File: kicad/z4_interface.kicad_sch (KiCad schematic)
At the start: 0 parts

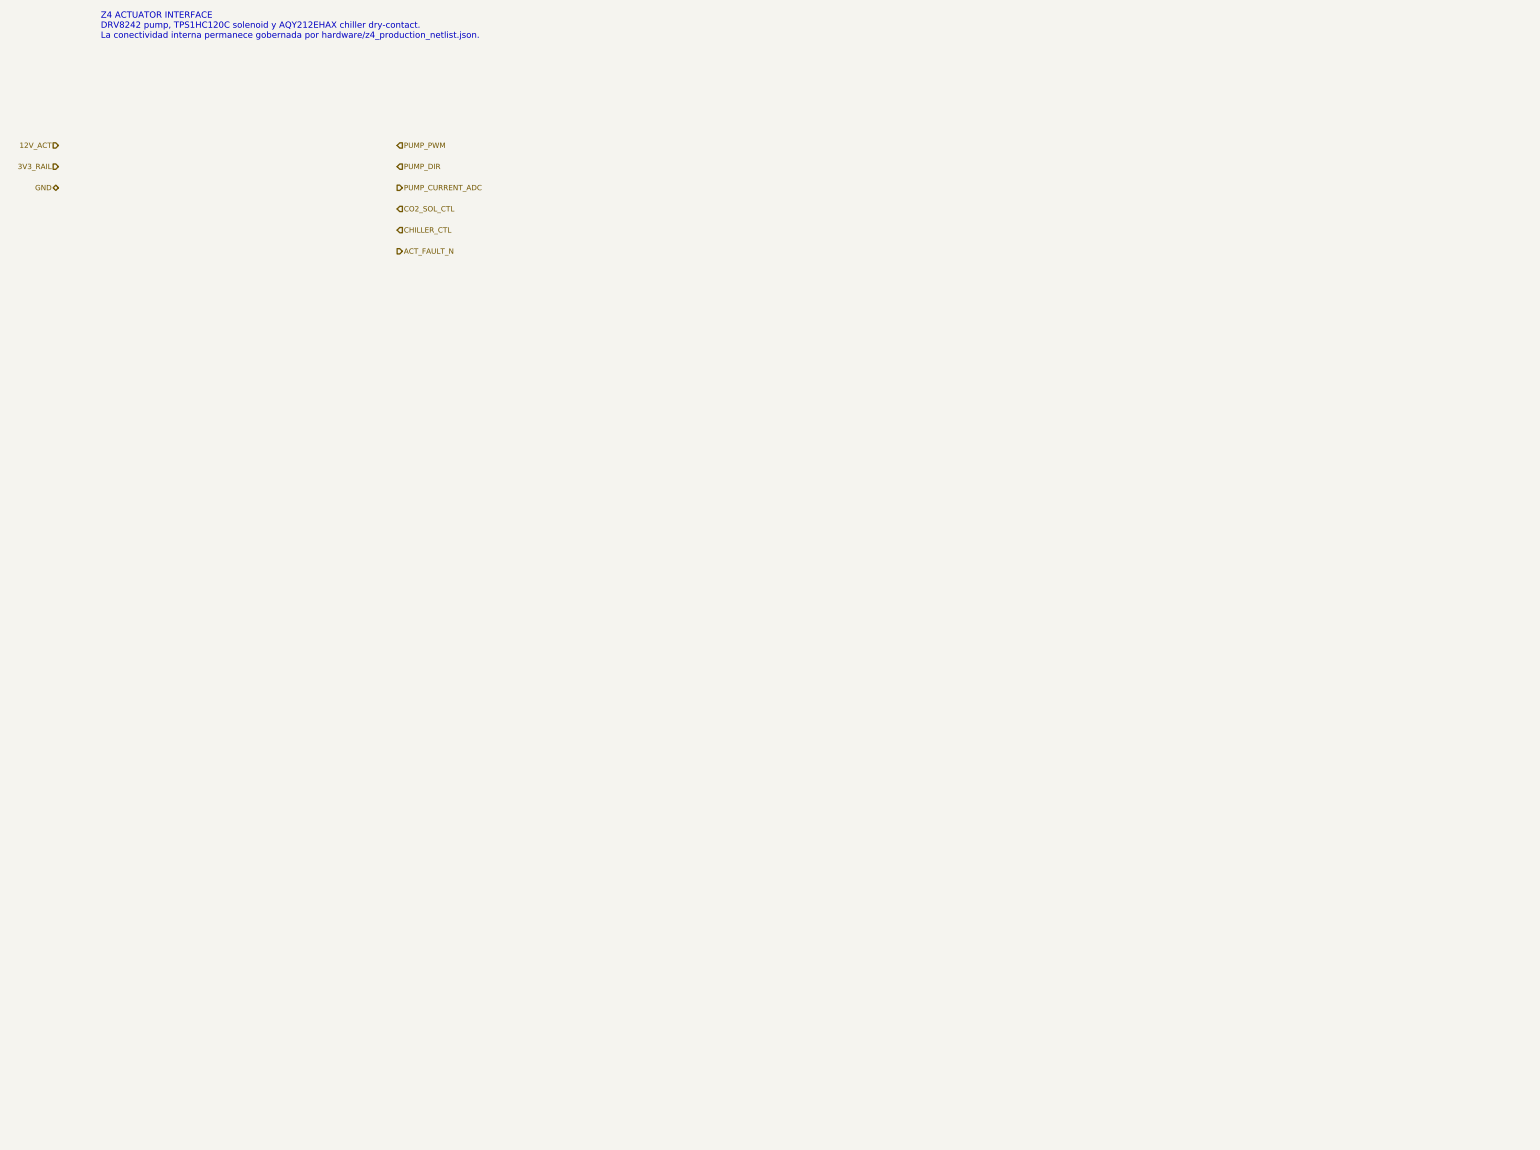
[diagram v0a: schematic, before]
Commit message: eda: materializar hierarchy de producción y cerrar ERC en cero (#15)
Materializa Z0–Z4 de forma determinista desde JSON/BOM, registra NFB_GEN, cierra seis links físicos verificados, elimina la deuda ERC de PR #14 y congela ERC=0/0 antes de placement. Mantiene placement, routing y geometría PCB fuera de alcance.
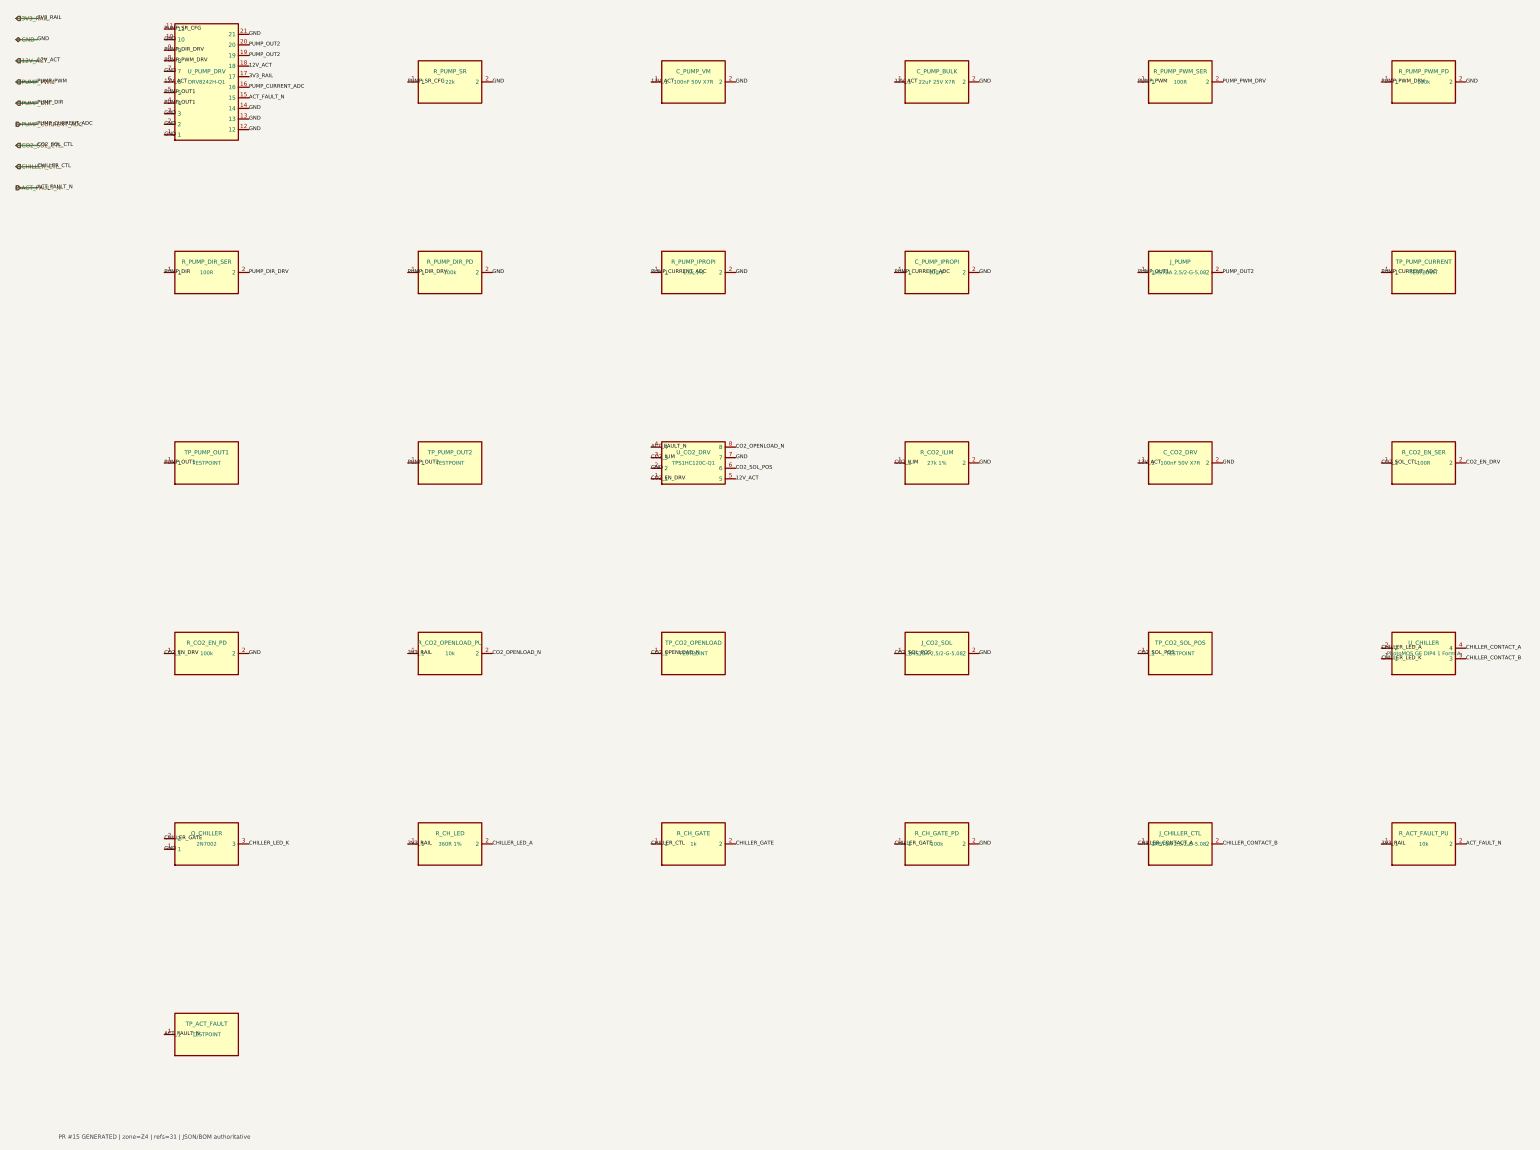
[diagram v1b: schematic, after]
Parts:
- added C_CO2_DRV: 100nF 50V X7R, Capacitor_SMD:C_0603_1608Metric, symbol NFB_GEN:SYM_C_CO2_DRV
- added C_PUMP_BULK: 22uF 25V X7R, Capacitor_SMD:C_1210_3225Metric, symbol NFB_GEN:SYM_C_PUMP_BULK
- added C_PUMP_IPROPI: 100nF, Capacitor_SMD:C_0402_1005Metric, symbol NFB_GEN:SYM_C_PUMP_IPROPI
- added C_PUMP_VM: 100nF 50V X7R, Capacitor_SMD:C_0603_1608Metric, symbol NFB_GEN:SYM_C_PUMP_VM
- added J_CHILLER_CTL: MSTBA 2,5/2-G-5.08, Connector_Phoenix_MSTB:PhoenixContact_MSTBA_2,5_2-G-5,08_1x02_P5.08mm_Horizontal, symbol NFB_GEN:SYM_J_CHILLER_CTL
- added J_CO2_SOL: MSTBA 2,5/2-G-5,08, Connector_Phoenix_MSTB:PhoenixContact_MSTBA_2,5_2-G-5,08_1x02_P5.08mm_Horizontal, symbol NFB_GEN:SYM_J_CO2_SOL
- added J_PUMP: MSTBA 2,5/2-G-5,08, Connector_Phoenix_MSTB:PhoenixContact_MSTBA_2,5_2-G-5,08_1x02_P5.08mm_Horizontal, symbol NFB_GEN:SYM_J_PUMP
- added Q_CHILLER: 2N7002, Package_TO_SOT_SMD:SOT-23, symbol NFB_GEN:SYM_Q_CHILLER
- added R_ACT_FAULT_PU: 10k, Resistor_SMD:R_0402_1005Metric, symbol NFB_GEN:SYM_R_ACT_FAULT_PU
- added R_CH_GATE: 1k, Resistor_SMD:R_0402_1005Metric, symbol NFB_GEN:SYM_R_CH_GATE
- added R_CH_GATE_PD: 100k, Resistor_SMD:R_0402_1005Metric, symbol NFB_GEN:SYM_R_CH_GATE_PD
- added R_CH_LED: 360R 1%, Resistor_SMD:R_0402_1005Metric, symbol NFB_GEN:SYM_R_CH_LED
- added R_CO2_EN_PD: 100k, Resistor_SMD:R_0402_1005Metric, symbol NFB_GEN:SYM_R_CO2_EN_PD
- added R_CO2_EN_SER: 100R, Resistor_SMD:R_0402_1005Metric, symbol NFB_GEN:SYM_R_CO2_EN_SER
- added R_CO2_ILIM: 27k 1%, Resistor_SMD:R_0402_1005Metric, symbol NFB_GEN:SYM_R_CO2_ILIM
- added R_CO2_OPENLOAD_PU: 10k, Resistor_SMD:R_0402_1005Metric, symbol NFB_GEN:SYM_R_CO2_OPENLOAD_PU
- added R_PUMP_DIR_PD: 100k, Resistor_SMD:R_0402_1005Metric, symbol NFB_GEN:SYM_R_PUMP_DIR_PD
- added R_PUMP_DIR_SER: 100R, Resistor_SMD:R_0402_1005Metric, symbol NFB_GEN:SYM_R_PUMP_DIR_SER
- added R_PUMP_IPROPI: 1.5k 1%, Resistor_SMD:R_0402_1005Metric, symbol NFB_GEN:SYM_R_PUMP_IPROPI
- added R_PUMP_PWM_PD: 100k, Resistor_SMD:R_0402_1005Metric, symbol NFB_GEN:SYM_R_PUMP_PWM_PD
- added R_PUMP_PWM_SER: 100R, Resistor_SMD:R_0402_1005Metric, symbol NFB_GEN:SYM_R_PUMP_PWM_SER
- added R_PUMP_SR: 22k, Resistor_SMD:R_0402_1005Metric, symbol NFB_GEN:SYM_R_PUMP_SR
- added TP_ACT_FAULT: TESTPOINT, TestPoint:TestPoint_Pad_D1.0mm, symbol NFB_GEN:SYM_TP_ACT_FAULT
- added TP_CO2_OPENLOAD: TESTPOINT, TestPoint:TestPoint_Pad_D1.0mm, symbol NFB_GEN:SYM_TP_CO2_OPENLOAD
- added TP_CO2_SOL_POS: TESTPOINT, TestPoint:TestPoint_Pad_D1.5mm, symbol NFB_GEN:SYM_TP_CO2_SOL_POS
- added TP_PUMP_CURRENT: TESTPOINT, TestPoint:TestPoint_Pad_D1.0mm, symbol NFB_GEN:SYM_TP_PUMP_CURRENT
- added TP_PUMP_OUT1: TESTPOINT, TestPoint:TestPoint_Pad_D1.5mm, symbol NFB_GEN:SYM_TP_PUMP_OUT1
- added TP_PUMP_OUT2: TESTPOINT, TestPoint:TestPoint_Pad_D1.5mm, symbol NFB_GEN:SYM_TP_PUMP_OUT2
- added U_CHILLER: PhotoMOS GE DIP4 1 Form A, NFB:Panasonic_AQY212EHAX_DIP4_SMD, symbol NFB_GEN:SYM_U_CHILLER
- added U_CO2_DRV: TPS1HC120C-Q1, NFB:TI_DYC0008A_TPS1HC120, symbol NFB_GEN:SYM_U_CO2_DRV
- added U_PUMP_DRV: DRV8242H-Q1, NFB:TI_RHL0020B_DRV8242, symbol NFB_GEN:SYM_U_PUMP_DRV
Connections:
- net 12V_ACT: now also C_CO2_DRV.1, C_PUMP_BULK.1, C_PUMP_VM.1, U_CO2_DRV.5, U_PUMP_DRV.18, U_PUMP_DRV.6
- net 3V3_RAIL: now also R_ACT_FAULT_PU.1, R_CH_LED.1, R_CO2_OPENLOAD_PU.1, U_PUMP_DRV.17
- net ACT_FAULT_N: now also R_ACT_FAULT_PU.2, TP_ACT_FAULT.1, U_CO2_DRV.4, U_PUMP_DRV.15
- net CHILLER_CTL: now also R_CH_GATE.1
- net CO2_SOL_CTL: now also R_CO2_EN_SER.1
- net GND: now also C_CO2_DRV.2, C_PUMP_BULK.2, C_PUMP_IPROPI.2, C_PUMP_VM.2, J_CO2_SOL.2, Q_CHILLER.1, R_CH_GATE_PD.2, R_CO2_EN_PD.2, R_CO2_ILIM.2, R_PUMP_DIR_PD.2, R_PUMP_IPROPI.2, R_PUMP_PWM_PD.2, R_PUMP_SR.2, U_CO2_DRV.2, U_CO2_DRV.7, U_PUMP_DRV.1, U_PUMP_DRV.10, U_PUMP_DRV.12, U_PUMP_DRV.13, U_PUMP_DRV.14, U_PUMP_DRV.2, U_PUMP_DRV.21, U_PUMP_DRV.3, U_PUMP_DRV.7
- net PUMP_CURRENT_ADC: now also C_PUMP_IPROPI.1, R_PUMP_IPROPI.1, TP_PUMP_CURRENT.1, U_PUMP_DRV.16
- net PUMP_DIR: now also R_PUMP_DIR_SER.1
- net PUMP_PWM: now also R_PUMP_PWM_SER.1
- new net CHILLER_CONTACT_A: J_CHILLER_CTL.1, U_CHILLER.4
- new net CHILLER_CONTACT_B: J_CHILLER_CTL.2, U_CHILLER.3
- new net CHILLER_GATE: Q_CHILLER.2, R_CH_GATE.2, R_CH_GATE_PD.1
- new net CHILLER_LED_A: R_CH_LED.2, U_CHILLER.2
- new net CHILLER_LED_K: Q_CHILLER.3, U_CHILLER.1
- new net CO2_EN_DRV: R_CO2_EN_PD.1, R_CO2_EN_SER.2, U_CO2_DRV.1
- new net CO2_ILIM: R_CO2_ILIM.1, U_CO2_DRV.3
- new net CO2_OPENLOAD_N: R_CO2_OPENLOAD_PU.2, TP_CO2_OPENLOAD.1, U_CO2_DRV.8
- new net CO2_SOL_POS: J_CO2_SOL.1, TP_CO2_SOL_POS.1, U_CO2_DRV.6
- new net PUMP_DIR_DRV: R_PUMP_DIR_PD.1, R_PUMP_DIR_SER.2, U_PUMP_DRV.9
- new net PUMP_OUT1: J_PUMP.1, TP_PUMP_OUT1.1, U_PUMP_DRV.4, U_PUMP_DRV.5
- new net PUMP_OUT2: J_PUMP.2, TP_PUMP_OUT2.1, U_PUMP_DRV.19, U_PUMP_DRV.20
- new net PUMP_PWM_DRV: R_PUMP_PWM_PD.1, R_PUMP_PWM_SER.2, U_PUMP_DRV.8
- new net PUMP_SR_CFG: R_PUMP_SR.1, U_PUMP_DRV.11
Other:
- note added: "PR #15 GENERATED | zone=Z4 | refs=31 | JSON/BOM authoritative"
- note removed: "Z4 ACTUATOR INTERFACE DRV8242 pump, TPS1HC120C solenoid y AQY212EHAX chiller dry-contact. La conectividad interna permanece gobernada por hardware/z4_production_netlist.json."
- title: NFB Insight PCBA v2 — Z4 Interface -> NFB Insight PCBA v2 — Z4 GENERATED PRODUCTION
